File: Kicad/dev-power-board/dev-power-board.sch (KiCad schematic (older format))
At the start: 22 parts, among them J10 Conn_01x02_Male, J11 Conn_02x03_Counter_Clockwise, J12 Conn_01x02_Male, J3 Conn_01x01_Male, J4 Conn_01x01_Male, J5 Conn_02x03_Counter_Clockwise, J6 Conn_01x02_Male, J7 Conn_01x02_Male, J8 Conn_02x03_Counter_Clockwise, J9 Conn_01x02_Male, U1 AMS1117-5.0, U2 AMS1117-3.3

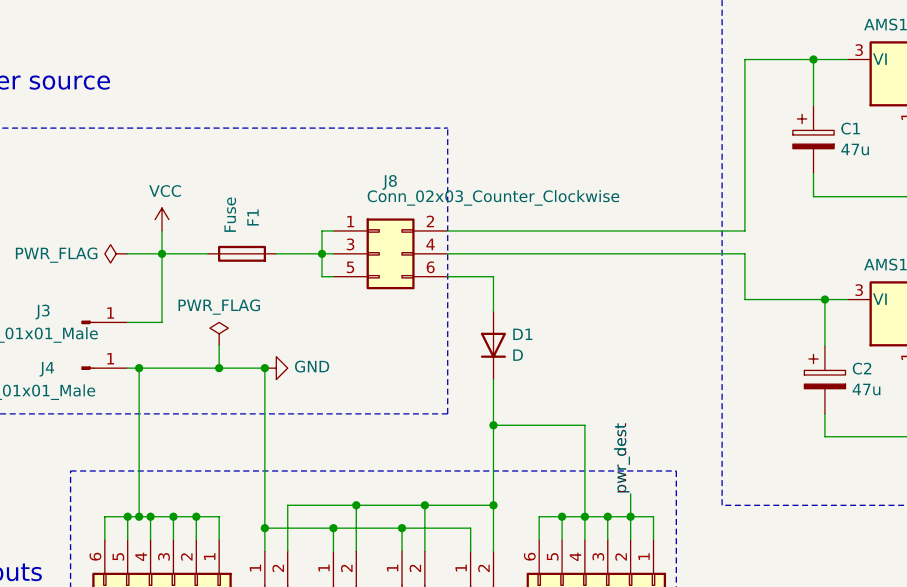
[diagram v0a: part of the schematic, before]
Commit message: Tracks width + silk
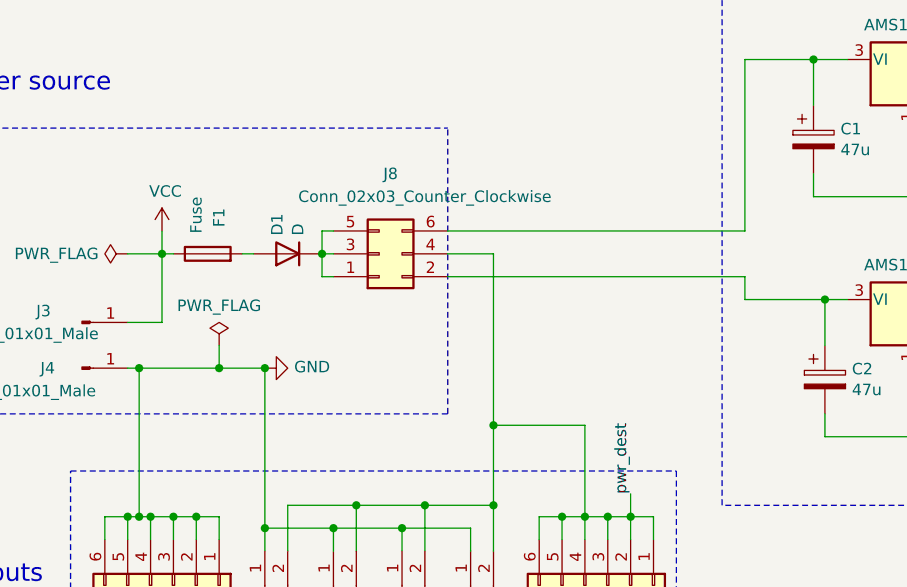
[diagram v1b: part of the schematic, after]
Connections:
- net pwr_dest: now also J8.4 (Pin_4); no longer D1.1 (K)
- net at J8.1 (Pin_1), J8.3 (Pin_3), J8.5 (Pin_5): now also D1.1 (K); no longer F1.2
- net at C1.1, U1.3 (VI): now also J8.6 (Pin_6); no longer J8.2 (Pin_2)
- net at C2.1, U2.3 (VI): now also J8.2 (Pin_2); no longer J8.4 (Pin_4)
- net at D1.2 (A): now also F1.2; no longer J8.6 (Pin_6)
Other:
- moved on the sheet: D1, F1
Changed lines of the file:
@@
-$EndComp
-$Comp
-L Device:D D1
-U 1 1 5F55460C
-P 4300 2650
-F 0 "D1" V 4346 2570 50  0000 R CNN
-F 1 "D" V 4255 2570 50  0000 R CNN
-F 2 "Diode_SMD:D_0805_2012Metric_Pad1.15x1.40mm_HandSolder" H 4300 2650 50  0001 C CNN
-F 3 "~" H 4300 2650 50  0001 C CNN
-	1    4300 2650
-	0    -1   -1   0
 $EndComp
 $Comp
@@
 	1    0    0    -1
 $EndComp
-$Comp
-L Connector_Generic:Conn_02x03_Odd_Even J8
-U 1 1 5F5506F5
-P 3800 2250
-F 0 "J8" H 3850 2567 50  0000 C CNN
-F 1 "Conn_02x03_Counter_Clockwise" H 4300 2500 50  0000 C CNN
-F 2 "Connector_PinHeader_2.54mm:PinHeader_2x03_P2.54mm_Vertical" H 3800 2250 50  0001 C CNN
-F 3 "~" H 3800 2250 50  0001 C CNN
-	1    3800 2250
-	1    0    0    -1
-$EndComp
-Wire Wire Line
-	4100 2250 5400 2250
-Wire Wire Line
-	4100 2150 5400 2150
 Wire Wire Line
 	5400 2150 5400 1400
@@
 	5400 1400 5700 1400
 Wire Wire Line
-	5400 2250 5400 2450
-Wire Wire Line
 	5400 2450 5750 2450
 Wire Wire Line
@@
 Wire Wire Line
 	7100 2450 6950 2450
-Wire Wire Line
-	4100 2350 4300 2350
-Wire Wire Line
-	4300 2350 4300 2500
 Wire Wire Line
 	5750 2950 5750 3050
@@
 Wire Wire Line
 	4300 3000 4700 3000
-Connection ~ 4300 3000
-Wire Wire Line
-	4300 3000 4300 2800
 Wire Wire Line
 	2850 2550 2700 2550
@@
 L Device:Fuse F1
 U 1 1 5F64FC82
-P 3200 2250
-F 0 "F1" H 3400 2200 50  0000 R CNN
-F 1 "Fuse" H 3450 2300 50  0000 R CNN
-F 2 "Fuse:Fuse_0805_2012Metric_Pad1.15x1.40mm_HandSolder" V 3130 2250 50  0001 C CNN
-F 3 "~" H 3200 2250 50  0001 C CNN
-	1    3200 2250
+P 3050 2250
+F 0 "F1" H 3250 2200 50  0000 R CNN
+F 1 "Fuse" H 3300 2300 50  0000 R CNN
+F 2 "Fuse:Fuse_0805_2012Metric_Pad1.15x1.40mm_HandSolder" V 2980 2250 50  0001 C CNN
+F 3 "~" H 3050 2250 50  0001 C CNN
+	1    3050 2250
 	0    -1   -1   0
 $EndComp
@@
 	2850 2150 2850 2250
 Wire Wire Line
-	3050 2250 2850 2250
+	2900 2250 2850 2250
 Connection ~ 2850 2250
 Wire Wire Line
-	3350 2250 3550 2250
+	3200 2250 3250 2250
 Wire Wire Line
 	2850 2250 2700 2250
@@
 Wire Notes Line
 	4100 2950 4100 1700
+$Comp
+L Connector_Generic:Conn_02x03_Odd_Even J8
+U 1 1 5F5506F5
+P 3800 2250
+F 0 "J8" H 3850 1900 50  0000 C CNN
+F 1 "Conn_02x03_Counter_Clockwise" H 4000 2000 50  0000 C CNN
+F 2 "Connector_PinHeader_2.54mm:PinHeader_2x03_P2.54mm_Vertical" H 3800 2250 50  0001 C CNN
+F 3 "~" H 3800 2250 50  0001 C CNN
+	1    3800 2250
+	1    0    0    1
+$EndComp
+Wire Wire Line
+	4100 2150 5400 2150
+Wire Wire Line
+	4100 2250 4300 2250
+Wire Wire Line
+	4100 2350 5400 2350
+Wire Wire Line
+	5400 2350 5400 2450
+$Comp
+L Device:D D1
+U 1 1 5F55460C
+P 3400 2250
+F 0 "D1" V 3446 2170 50  0000 R CNN
+F 1 "D" V 3355 2170 50  0000 R CNN
+F 2 "Diode_SMD:D_0805_2012Metric_Pad1.15x1.40mm_HandSolder" H 3400 2250 50  0001 C CNN
+F 3 "~" H 3400 2250 50  0001 C CNN
+	1    3400 2250
+	-1   0    0    1
+$EndComp
+Wire Wire Line
+	4300 2250 4300 3000
+Connection ~ 4300 3000
 $EndSCHEMATC
